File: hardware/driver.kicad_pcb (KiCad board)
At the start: 2 copper layers, 24 x 23 mm, 15 parts, among them Q1 BSS84, Q2 BSS138, Q3 BSS138, Q4 BSS84, Q5 BSS138, Q6 BSS138

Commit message: Routing
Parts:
- moved R1 0.25 mm to (103.0, 70.0), turned to 90 degrees
- turned Q1 to 90 degrees
- turned Q4 to 90 degrees
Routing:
- net VCC: track 0.00 -> 30.1 mm
- net GND: track 0.00 -> 12.6 mm, vias 0 -> 10
- net Net-(Q1-Pad1): track 0.00 -> 10.7 mm, vias 0 -> 2
- net Net-(Q4-Pad1): track 0.00 -> 10.4 mm, vias 0 -> 2
- net Net-(Q2-Pad1): track 0.00 -> 9.47 mm, vias 0 -> 2
- net Net-(Q4-Pad3): track 0.00 -> 9.04 mm
- net Net-(Q1-Pad3): track 0.00 -> 9.00 mm
- net Net-(Q5-Pad1): track 0.00 -> 6.85 mm
- added copper zone on B.Cu, net GND

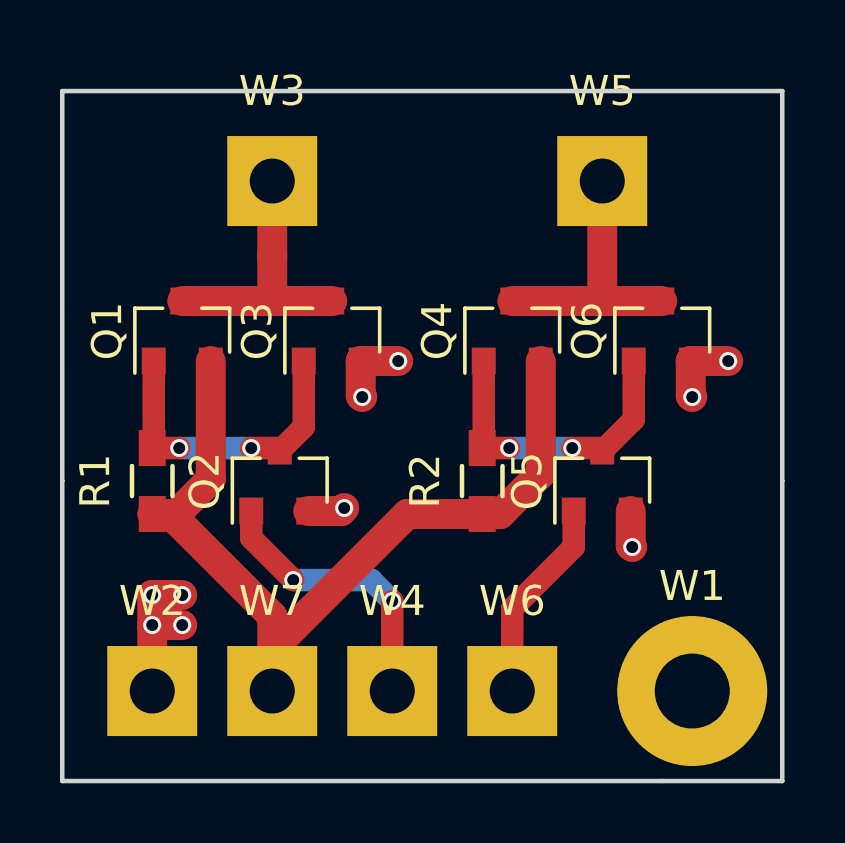
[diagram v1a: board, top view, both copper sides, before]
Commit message: Added optional RC filter
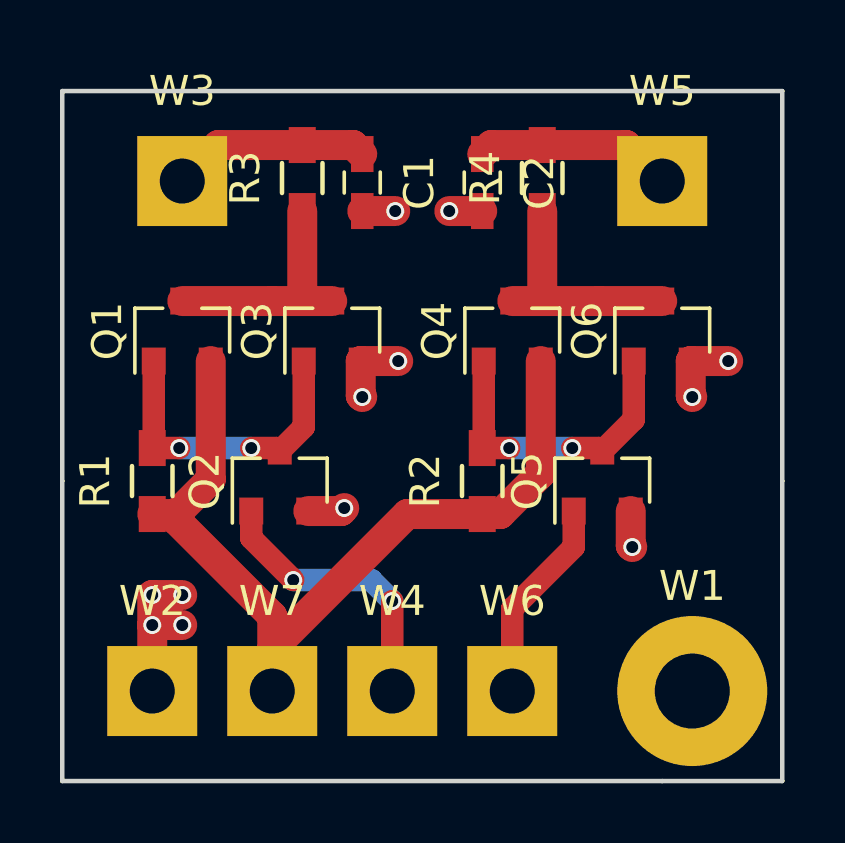
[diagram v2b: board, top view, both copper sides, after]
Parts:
- added C1: C, Capacitors_SMD:C_0603_HandSoldering, F.Cu at (110.0, 60.0)
- added C2: C, Capacitors_SMD:C_0603_HandSoldering, F.Cu at (114.0, 60.0)
- added R3: R, Resistors_SMD:R_0603_HandSoldering, F.Cu at (108.0, 59.9)
- added R4: R, Resistors_SMD:R_0603_HandSoldering, F.Cu at (116.0, 59.9)
- moved W3 3.00 mm to (104.0, 60.0)
- moved W5 2.00 mm to (120.0, 60.0)
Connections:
- W3 pad 1: Net-(Q1-Pad3) -> Net-(C1-Pad1)
- W5 pad 1: Net-(Q4-Pad3) -> Net-(C2-Pad1)
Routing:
- net Net-(C2-Pad1): track 0.00 -> 6.62 mm
- net Net-(C1-Pad1): track 0.00 -> 6.62 mm
- net GND: track 12.6 -> 14.8 mm, vias 10 -> 12
- net Net-(Q4-Pad3): track 9.04 -> 8.00 mm
- net Net-(Q1-Pad3): track 9.00 -> 8.00 mm

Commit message: Added logo
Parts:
- added G***: LOGO, Keio:logo2_16x5mm_flipped, F.Cu at (112.0, 65.1)

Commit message: Top silk
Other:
- board text added: "+"
- board text added: "1"
- board text added: "2"
- board text added: "C"
- board text added: "G"
- board text added: "Q1"
- board text added: "Q2"
- board text added: "Q3"
- board text added: "Q4"
- board text added: "Q5"
- board text added: "Q6"
- board text added: "R1"
- board text added: "R2"
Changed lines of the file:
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@@
     (area 99.924999 56.924999 124.075001 80.075001)
     (thickness 1.6)
-    (drawings 7)
+    (drawings 22)
     (tracks 87)
     (zones 0)
@@
   (page A4)
   (layers
-    (0 F.Cu signal hide)
+    (0 F.Cu signal)
     (31 B.Cu signal)
     (32 B.Adhes user)
@@
     (pad_to_mask_clearance 0.2)
     (aux_axis_origin 0 0)
-    (visible_elements FFFCFD7F)
+    (visible_elements FFFEFF7F)
     (pcbplotparams
       (layerselection 0x00030_80000001)
@@
       (xy -2.796116 -1.725084) (xy -2.797198 -2.094474) (xy -2.798279 -2.463863) (xy -0.037064 -2.46272)) (layer Eco2.User) (width 0.01))
   )
+  (gr_text 2 (at 114 74 360) (layer Eco1.User)
+    (effects (font (size 1.5 1.5) (thickness 0.3)))
+  )
+  (gr_text 1 (at 110 74) (layer Eco1.User)
+    (effects (font (size 1.5 1.5) (thickness 0.3)))
+  )
+  (gr_text + (at 106 73.9) (layer Eco1.User)
+    (effects (font (size 1.5 1.5) (thickness 0.3)))
+  )
+  (gr_text G (at 102 74) (layer Eco1.User)
+    (effects (font (size 1.5 1.5) (thickness 0.3)))
+  )
+  (gr_text C (at 112 60 360) (layer Eco1.User)
+    (effects (font (size 1.3 1.3) (thickness 0.2)))
+  )
+  (gr_text R2 (at 112.4 70 90) (layer Eco1.User)
+    (effects (font (size 1.3 1.3) (thickness 0.2)))
+  )
+  (gr_text R1 (at 101.4 70 90) (layer Eco1.User)
+    (effects (font (size 1.3 1.3) (thickness 0.2)))
+  )
+  (gr_text Q2 (at 110.3 69) (layer Eco1.User)
+    (effects (font (size 1.3 1.3) (thickness 0.2)))
+  )
+  (gr_text Q5 (at 121 69) (layer Eco1.User)
+    (effects (font (size 1.3 1.3) (thickness 0.2)))
+  )
+  (gr_text Q6 (at 117.7 63) (layer Eco1.User)
+    (effects (font (size 1.3 1.3) (thickness 0.2)))
+  )
+  (gr_text Q4 (at 112.7 63) (layer Eco1.User)
+    (effects (font (size 1.3 1.3) (thickness 0.2)))
+  )
+  (gr_text Q3 (at 106.7 63) (layer Eco1.User)
+    (effects (font (size 1.3 1.3) (thickness 0.2)))
+  )
+  (gr_text Q1 (at 101.8 63) (layer Eco1.User)
+    (effects (font (size 1.3 1.3) (thickness 0.2)))
+  )
+  (gr_text 2 (at 122.8 60 360) (layer Eco1.User)
+    (effects (font (size 1.5 1.5) (thickness 0.3)))
+  )
+  (gr_text 1 (at 101.2 60) (layer Eco1.User)
+    (effects (font (size 1.5 1.5) (thickness 0.3)))
+  )
   (gr_line (start 100 57) (end 100 70) (layer Edge.Cuts) (width 0.15))
